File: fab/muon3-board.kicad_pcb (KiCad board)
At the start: 2 copper layers, 160 x 120 mm, 4 parts

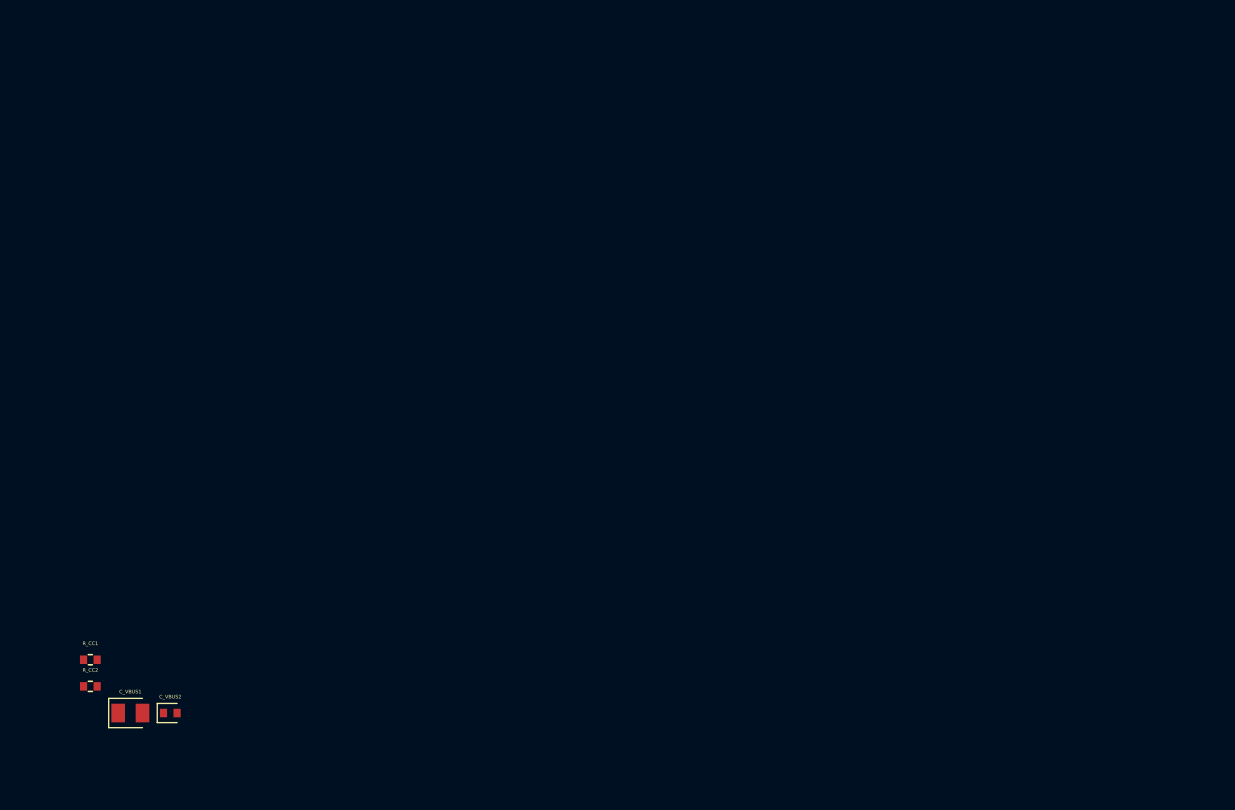
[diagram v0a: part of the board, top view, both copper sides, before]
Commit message: board: author AFE channel 0 as real board-as-code (OPA858 + dual TLV3601)
First subsystem authored end-to-end with vendored exact JLC parts and a
verified netlist, per the "one subsystem fully correct" plan.

board/afe.tsx — one AFE channel wired from sim/circuit/afe_hamamatsu_s12572.cir:
- OPA858 TIA: IN_NEG = summing node (INA), IN_POS = VBOT ref, Rf 15k ‖ Cf
  1.5p on the FB pin (FB is internally tied to OUT per the TI datasheet —
  lower-parasitic feedback), OUT drives the comparators, PD tied high.
- 1N4148W (C2128) rail clamps on INA to VANA/GND (unambiguous vs a 3-pin
  BAV99, which imported as a generic diode).
- dual TLV3601 (C2974371): signal on IN_POS, DAC threshold (RC-filtered) on
  IN_NEG; outputs via 33Ω/6p to the FPGA header.
- panel hybrid connector (SiPM SIG/HV/GND/cold+hot NTC) and per-rail
  decoupling. Layout generously spaced — no pad/courtyard overlaps.

Netlist verified from circuit-json: INA0 = {Rser, OPA858 IN_NEG, Rf, Cf,
both clamps}; FB0 = {OPA858 FB, Rf, Cf}; AOUT0 = {OPA858 OUT, both cmp
IN_POS, FPGA}; thresholds/bias/rails all correct.

fab/ regenerated: 27 placements, 14 BOM line items, every part with a real
JLCPCB number. DRC-clean (Circuits 1 passed).

Co-Authored-By: Claude Opus 4.8 <noreply@anthropic.com>
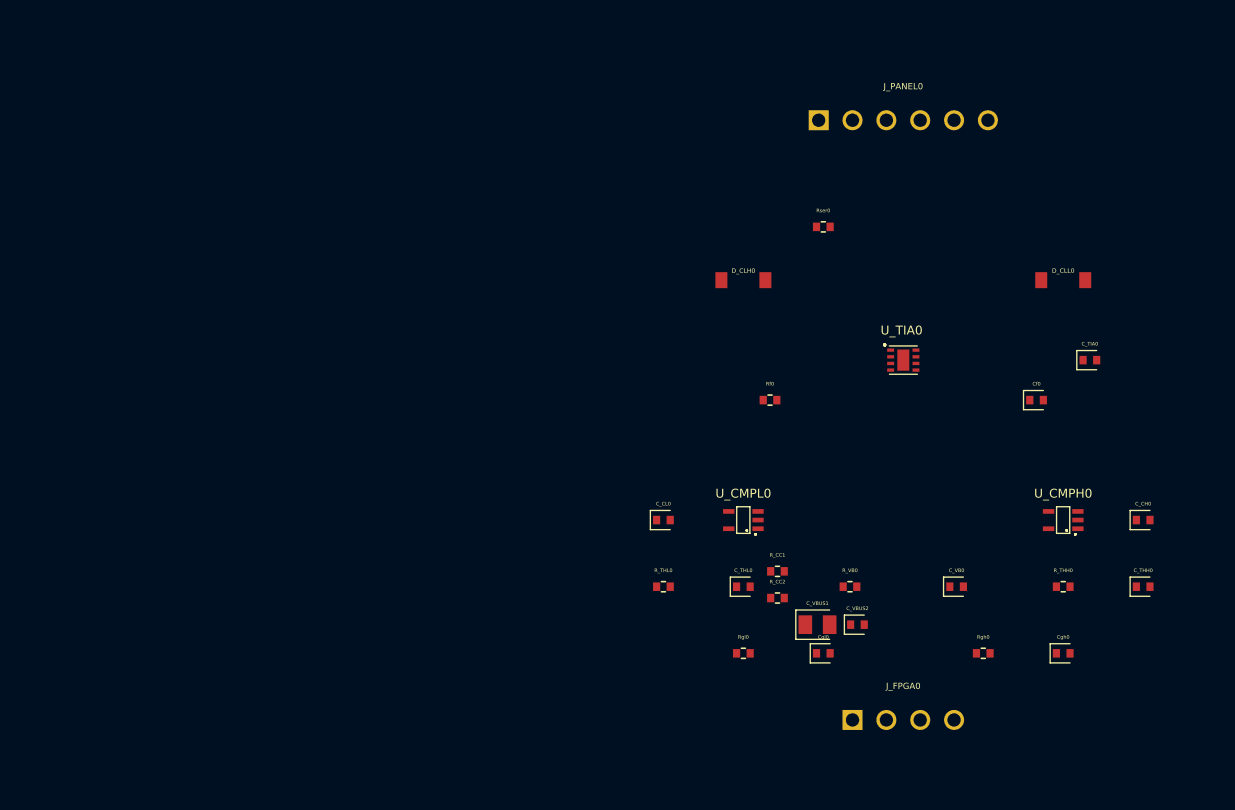
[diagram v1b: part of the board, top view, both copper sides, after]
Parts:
- added C_CH0: 100nF, tscircuit:capacitor_0402, F.Cu at (116.0, 133.5)
- added C_CL0: 100nF, tscircuit:capacitor_0402, F.Cu at (80.0, 133.5)
- added C_THH0: 100nF, tscircuit:capacitor_0402, F.Cu at (116.0, 138.5)
- added C_THL0: 100nF, tscircuit:capacitor_0402, F.Cu at (86.0, 138.5)
- added C_TIA0: 100nF, tscircuit:capacitor_0402, F.Cu at (112.0, 121.5)
- added C_VB0: 100nF, tscircuit:capacitor_0402, F.Cu at (102.0, 138.5)
- added Cf0: 1.5pF, tscircuit:capacitor_0402, F.Cu at (108.0, 124.5)
- added Cgh0: 6pF, tscircuit:capacitor_0402, F.Cu at (110.0, 143.5)
- added Cgl0: 6pF, tscircuit:capacitor_0402, F.Cu at (92.0, 143.5)
- added D_CLH0: D, tscircuit:diode_sod123, F.Cu at (86.0, 115.5)
- added D_CLL0: D, tscircuit:diode_sod123, F.Cu at (110.0, 115.5)
- added J_FPGA0: J_FPGA0, tscircuit:pin_header_pinrow4_nopinlabels, F.Cu at (98.0, 148.5)
- added J_PANEL0: J_PANEL0, tscircuit:pin_header_pinrow6_nopinlabels_female, F.Cu at (98.0, 103.5)
- added R_THH0: 1kΩ, tscircuit:resistor_res0402, F.Cu at (110.0, 138.5)
- added R_THL0: 1kΩ, tscircuit:resistor_res0402, F.Cu at (80.0, 138.5)
- added R_VB0: 1kΩ, tscircuit:resistor_res0402, F.Cu at (94.0, 138.5)
- added Rf0: 15kΩ, tscircuit:resistor_res0402, F.Cu at (88.0, 124.5)
- added Rgh0: 33Ω, tscircuit:resistor_res0402, F.Cu at (104.0, 143.5)
- added Rgl0: 33Ω, tscircuit:resistor_res0402, F.Cu at (86.0, 143.5)
- added Rser0: 10Ω, tscircuit:resistor_res0402, F.Cu at (92.0, 111.5)
- added U_CMPH0: TLV3601DCKR, tscircuit:TLV3601DCKR, F.Cu at (110.0, 133.5)
- added U_CMPL0: TLV3601DCKR, tscircuit:TLV3601DCKR, F.Cu at (86.0, 133.5)
- added U_TIA0: OPA858IDSGR, tscircuit:OPA858IDSGR, F.Cu at (98.0, 121.5)
- moved C_VBUS1 52.0 mm to (91.6, 141.4)
- moved C_VBUS2 52.0 mm to (94.6, 141.4)
- moved R_CC1 52.0 mm to (88.6, 137.4)
- moved R_CC2 52.0 mm to (88.6, 139.4)
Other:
- board text added: "+"
- board text added: "-"

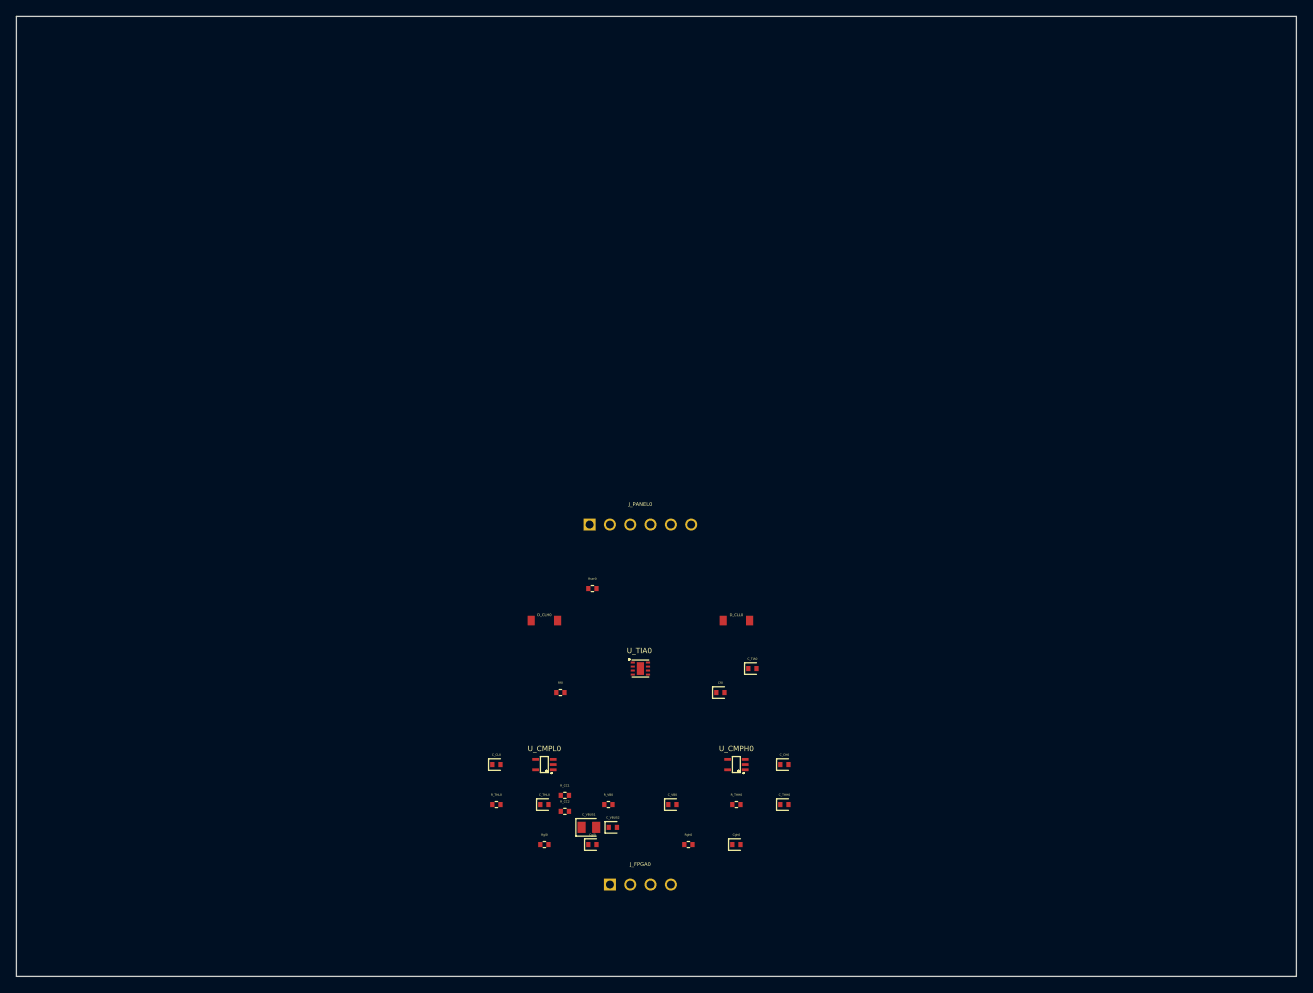
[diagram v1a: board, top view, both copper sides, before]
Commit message: board: 4-layer floorplan + AFE x4 placement (power/size/trace-width aware)
Design the placement for the 160x120 4-layer board from the frozen
requirements (pcb/SCHEMATIC_FREEZE_CHECK.md, DESIGN_RULES.md).

- board/layout.ts: single-source floorplan — 4-layer stackup, six zones
  (RF | AFE x4 | HV over DIGITAL / POWER / TEC), AFE channel anchors,
  antenna keepout, M3 holes, and a net-class trace-width table (12V TEC
  1.5mm pour, per-TEC/TEC-out 0.8mm @2.5A, 5V_A star 0.4mm, HV 0.25mm
  + 0.6mm creepage, RF 0.30mm 50R, ...).
- board/floorplan.tsx: renders zone fences, labels, shield/keepout notes,
  the quiet-top/noisy-bottom divider, and the four mounting holes.
- board/afe.tsx: recompiled each AFE channel into a compact ~18x40mm
  vertical strip (cable -> TIA -> comparators -> FPGA) and tiled all four
  across the AFE zone at 23mm pitch; DRC-clean, zero pad/courtyard overlaps.
- board/hv.tsx: LT3482 anchor placed in the HV zone (real vendored part).
- board/index.tsx: layers=4; composes floorplan + AFE x4 + power seed + HV.
- Fix: every <group> now carries pcbX/pcbY so tscircuit honors manual
  placement instead of auto-packing children to the board center.
- tools/fab.ts: per-step isolation so one failing export can't abort the
  run; tscircuit's gerber exporter rejects 4-layer inner layers, so gerbers
  are skipped and the KiCad export is the 4-layer fab source.
- board/LAYOUT.md: full placement design (stackup, zone rationale, power
  paths + currents, trace widths, isolation/keepout rules).

Placement principle: quiet upper half (RF/AFE/HV/digital) over a noisy
lower half (PD/TEC), continuous L2 ground, AFE summing nodes >=25mm from
switching, panel connectors on the top edge for short SiPM paths.
102 placements, 18 BOM line items, DRC-clean.

Co-Authored-By: Claude Opus 4.8 <noreply@anthropic.com>
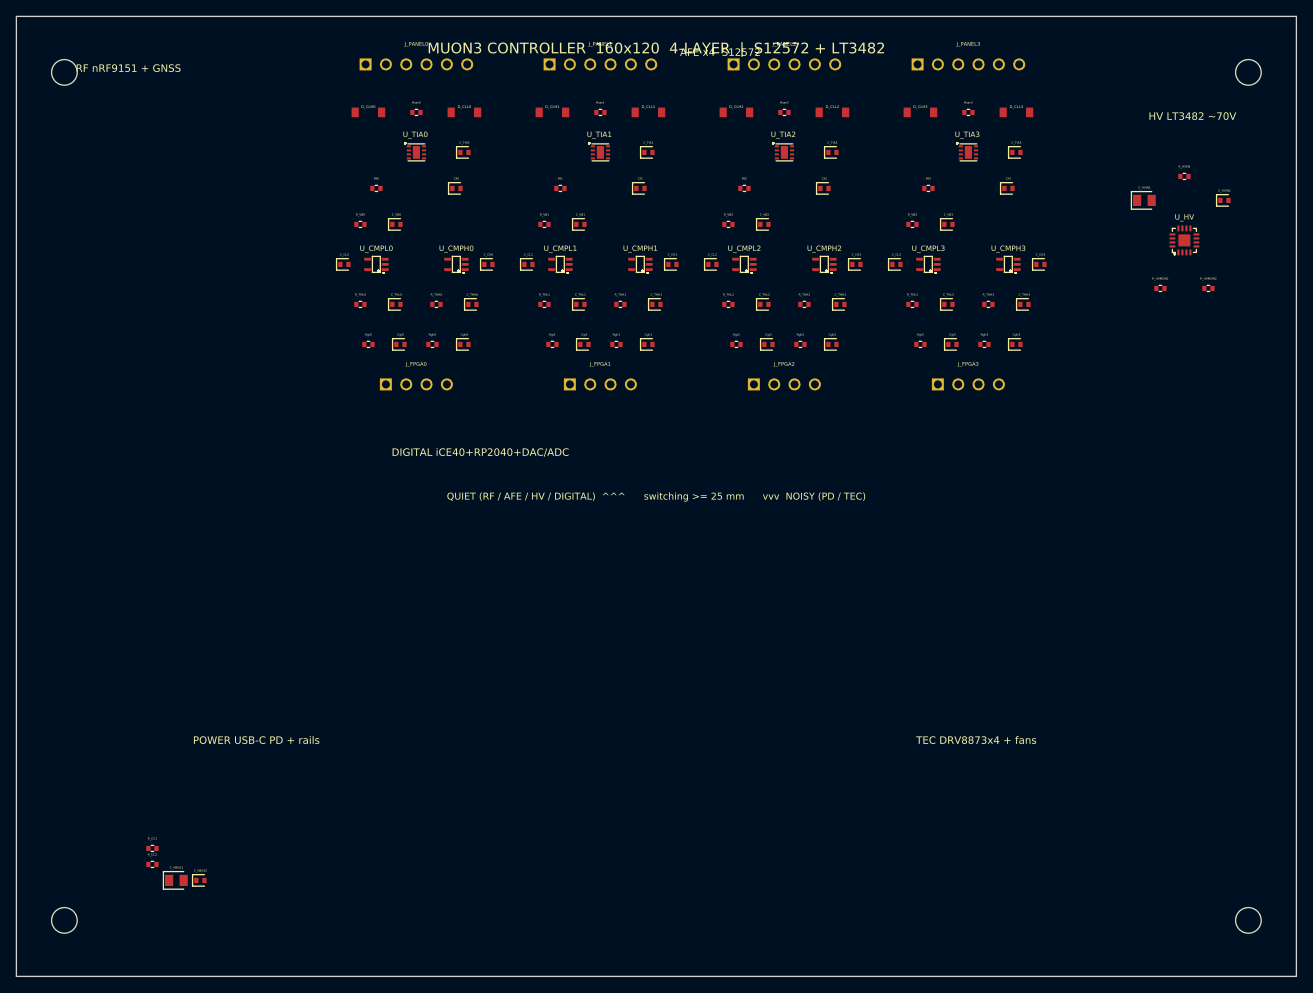
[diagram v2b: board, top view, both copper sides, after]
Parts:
- added ?: , tscircuit:hole_circle_holeDiameter3.2mm, F.Cu at (26.0, 47.0)
- added ?: , tscircuit:hole_circle_holeDiameter3.2mm, F.Cu at (174.0, 47.0)
- added ?: , tscircuit:hole_circle_holeDiameter3.2mm, F.Cu at (26.0, 153.0)
- added ?: , tscircuit:hole_circle_holeDiameter3.2mm, F.Cu at (174.0, 153.0)
- added C_CH1: 100nF, tscircuit:capacitor_0402, F.Cu at (102.0, 71.0)
- added C_CH2: 100nF, tscircuit:capacitor_0402, F.Cu at (125.0, 71.0)
- added C_CH3: 100nF, tscircuit:capacitor_0402, F.Cu at (148.0, 71.0)
- added C_CL1: 100nF, tscircuit:capacitor_0402, F.Cu at (84.0, 71.0)
- added C_CL2: 100nF, tscircuit:capacitor_0402, F.Cu at (107.0, 71.0)
- added C_CL3: 100nF, tscircuit:capacitor_0402, F.Cu at (130.0, 71.0)
- added C_HVIN1: 10uF, tscircuit:capacitor_0805, F.Cu at (161.0, 63.0)
- added C_HVIN2: 100nF, tscircuit:capacitor_0402, F.Cu at (171.0, 63.0)
- added C_THH1: 100nF, tscircuit:capacitor_0402, F.Cu at (100.0, 76.0)
- added C_THH2: 100nF, tscircuit:capacitor_0402, F.Cu at (123.0, 76.0)
- added C_THH3: 100nF, tscircuit:capacitor_0402, F.Cu at (146.0, 76.0)
- added C_THL1: 100nF, tscircuit:capacitor_0402, F.Cu at (90.5, 76.0)
- added C_THL2: 100nF, tscircuit:capacitor_0402, F.Cu at (113.5, 76.0)
- added C_THL3: 100nF, tscircuit:capacitor_0402, F.Cu at (136.5, 76.0)
- added C_TIA1: 100nF, tscircuit:capacitor_0402, F.Cu at (99.0, 57.0)
- added C_TIA2: 100nF, tscircuit:capacitor_0402, F.Cu at (122.0, 57.0)
- added C_TIA3: 100nF, tscircuit:capacitor_0402, F.Cu at (145.0, 57.0)
- added C_VB1: 100nF, tscircuit:capacitor_0402, F.Cu at (90.5, 66.0)
- added C_VB2: 100nF, tscircuit:capacitor_0402, F.Cu at (113.5, 66.0)
- added C_VB3: 100nF, tscircuit:capacitor_0402, F.Cu at (136.5, 66.0)
- added Cf1: 1.5pF, tscircuit:capacitor_0402, F.Cu at (98.0, 61.5)
- added Cf2: 1.5pF, tscircuit:capacitor_0402, F.Cu at (121.0, 61.5)
- added Cf3: 1.5pF, tscircuit:capacitor_0402, F.Cu at (144.0, 61.5)
- added Cgh1: 6pF, tscircuit:capacitor_0402, F.Cu at (99.0, 81.0)
- added Cgh2: 6pF, tscircuit:capacitor_0402, F.Cu at (122.0, 81.0)
- added Cgh3: 6pF, tscircuit:capacitor_0402, F.Cu at (145.0, 81.0)
- added Cgl1: 6pF, tscircuit:capacitor_0402, F.Cu at (91.0, 81.0)
- added Cgl2: 6pF, tscircuit:capacitor_0402, F.Cu at (114.0, 81.0)
- added Cgl3: 6pF, tscircuit:capacitor_0402, F.Cu at (137.0, 81.0)
- added D_CLH1: D, tscircuit:diode_sod123, F.Cu at (87.0, 52.0)
- added D_CLH2: D, tscircuit:diode_sod123, F.Cu at (110.0, 52.0)
- added D_CLH3: D, tscircuit:diode_sod123, F.Cu at (133.0, 52.0)
- added D_CLL1: D, tscircuit:diode_sod123, F.Cu at (99.0, 52.0)
- added D_CLL2: D, tscircuit:diode_sod123, F.Cu at (122.0, 52.0)
- added D_CLL3: D, tscircuit:diode_sod123, F.Cu at (145.0, 52.0)
- added J_FPGA1: J_FPGA1, tscircuit:pin_header_pinrow4_nopinlabels, F.Cu at (93.0, 86.0)
- added J_FPGA2: J_FPGA2, tscircuit:pin_header_pinrow4_nopinlabels, F.Cu at (116.0, 86.0)
- added J_FPGA3: J_FPGA3, tscircuit:pin_header_pinrow4_nopinlabels, F.Cu at (139.0, 86.0)
- added J_PANEL1: J_PANEL1, tscircuit:pin_header_pinrow6_nopinlabels_female, F.Cu at (93.0, 46.0)
- added J_PANEL2: J_PANEL2, tscircuit:pin_header_pinrow6_nopinlabels_female, F.Cu at (116.0, 46.0)
- added J_PANEL3: J_PANEL3, tscircuit:pin_header_pinrow6_nopinlabels_female, F.Cu at (139.0, 46.0)
- added R_HVEN: 100kΩ, tscircuit:resistor_res0402, F.Cu at (166.0, 60.0)
- added R_HVMON1: 2MΩ, tscircuit:resistor_res0402, F.Cu at (163.0, 74.0)
- added R_HVMON2: 51kΩ, tscircuit:resistor_res0402, F.Cu at (169.0, 74.0)
- added R_THH1: 1kΩ, tscircuit:resistor_res0402, F.Cu at (95.5, 76.0)
- added R_THH2: 1kΩ, tscircuit:resistor_res0402, F.Cu at (118.5, 76.0)
- added R_THH3: 1kΩ, tscircuit:resistor_res0402, F.Cu at (141.5, 76.0)
- added R_THL1: 1kΩ, tscircuit:resistor_res0402, F.Cu at (86.0, 76.0)
- added R_THL2: 1kΩ, tscircuit:resistor_res0402, F.Cu at (109.0, 76.0)
- added R_THL3: 1kΩ, tscircuit:resistor_res0402, F.Cu at (132.0, 76.0)
- added R_VB1: 1kΩ, tscircuit:resistor_res0402, F.Cu at (86.0, 66.0)
- added R_VB2: 1kΩ, tscircuit:resistor_res0402, F.Cu at (109.0, 66.0)
- added R_VB3: 1kΩ, tscircuit:resistor_res0402, F.Cu at (132.0, 66.0)
- added Rf1: 15kΩ, tscircuit:resistor_res0402, F.Cu at (88.0, 61.5)
- added Rf2: 15kΩ, tscircuit:resistor_res0402, F.Cu at (111.0, 61.5)
- added Rf3: 15kΩ, tscircuit:resistor_res0402, F.Cu at (134.0, 61.5)
- added Rgh1: 33Ω, tscircuit:resistor_res0402, F.Cu at (95.0, 81.0)
- added Rgh2: 33Ω, tscircuit:resistor_res0402, F.Cu at (118.0, 81.0)
- added Rgh3: 33Ω, tscircuit:resistor_res0402, F.Cu at (141.0, 81.0)
- added Rgl1: 33Ω, tscircuit:resistor_res0402, F.Cu at (87.0, 81.0)
- added Rgl2: 33Ω, tscircuit:resistor_res0402, F.Cu at (110.0, 81.0)
- added Rgl3: 33Ω, tscircuit:resistor_res0402, F.Cu at (133.0, 81.0)
- added Rser1: 10Ω, tscircuit:resistor_res0402, F.Cu at (93.0, 52.0)
- added Rser2: 10Ω, tscircuit:resistor_res0402, F.Cu at (116.0, 52.0)
- added Rser3: 10Ω, tscircuit:resistor_res0402, F.Cu at (139.0, 52.0)
- added U_CMPH1: TLV3601DCKR, tscircuit:TLV3601DCKR, F.Cu at (98.0, 71.0)
- added U_CMPH2: TLV3601DCKR, tscircuit:TLV3601DCKR, F.Cu at (121.0, 71.0)
- added U_CMPH3: TLV3601DCKR, tscircuit:TLV3601DCKR, F.Cu at (144.0, 71.0)
- added U_CMPL1: TLV3601DCKR, tscircuit:TLV3601DCKR, F.Cu at (88.0, 71.0)
- added U_CMPL2: TLV3601DCKR, tscircuit:TLV3601DCKR, F.Cu at (111.0, 71.0)
- added U_CMPL3: TLV3601DCKR, tscircuit:TLV3601DCKR, F.Cu at (134.0, 71.0)
- added U_HV: LT3482EUD_TRPBF, tscircuit:LT3482EUD_TRPBF, F.Cu at (166.0, 68.0)
- added U_TIA1: OPA858IDSGR, tscircuit:OPA858IDSGR, F.Cu at (93.0, 57.0)
- added U_TIA2: OPA858IDSGR, tscircuit:OPA858IDSGR, F.Cu at (116.0, 57.0)
- added U_TIA3: OPA858IDSGR, tscircuit:OPA858IDSGR, F.Cu at (139.0, 57.0)
- moved C_VB0 80.3 mm to (67.5, 66.0)
- moved R_VB0 78.9 mm to (63.0, 66.0)
- moved C_TIA0 73.9 mm to (76.0, 57.0)
- moved C_THH0 73.7 mm to (77.0, 76.0)
- moved R_THH0 72.9 mm to (72.5, 76.0)
- moved C_CH0 72.6 mm to (79.0, 71.0)
- moved D_CLL0 72.0 mm to (76.0, 52.0)
- moved U_CMPH0 71.7 mm to (75.0, 71.0)
- moved Cgh0 71.2 mm to (76.0, 81.0)
- moved Cf0 71.1 mm to (75.0, 61.5)
- moved U_TIA0 70.3 mm to (70.0, 57.0)
- moved Rgh0 70.2 mm to (72.0, 81.0)
- moved J_FPGA0 68.5 mm to (70.0, 86.0)
- moved D_CLH0 67.2 mm to (64.0, 52.0)
- moved Rf0 67.1 mm to (65.0, 61.5)
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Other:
- copper layers 2 -> 4
- board text added: "AFE shield fence over TIA banks; GND stitch 1 mm"
- board text added: "AFE x4 S12572"
- board text added: "ANT KEEPOUT R12mm"
- board text added: "DIGITAL iCE40+RP2040+DAC/ADC"
- board text added: "HV LT3482 ~70V"
- board text added: "MUON3 CONTROLLER 160x120 4-LAYER | S12572 + LT3482"
- board text added: "POWER USB-C PD + rails"
- board text added: "QUIET (RF / AFE / HV / DIGITAL) ^^^ switching >= 25 mm vvv NOISY (PD / TEC)"
- board text added: "RF nRF9151 + GNSS"
- board text added: "TEC DRV8873x4 + fans"
- board text added: "antenna keepout 12 mm; Nordic ref geometry"
- board text added: "no pour under SW node; 0.6 mm creepage @70V"
- board text added: "switching zone; short loops; keep >=25 mm from AFE"
